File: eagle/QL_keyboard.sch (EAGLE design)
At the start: 42 parts, among them J1 USB-A-S, J2 AVR_SPI_PRG_6TESTPOINTS, U2 3.3V/150mA, U3 MAX3421ESMD, U4 ATMEGA328P_TQFP, U5 TXB0108PW-TSSOP20, Y1 8MHZ

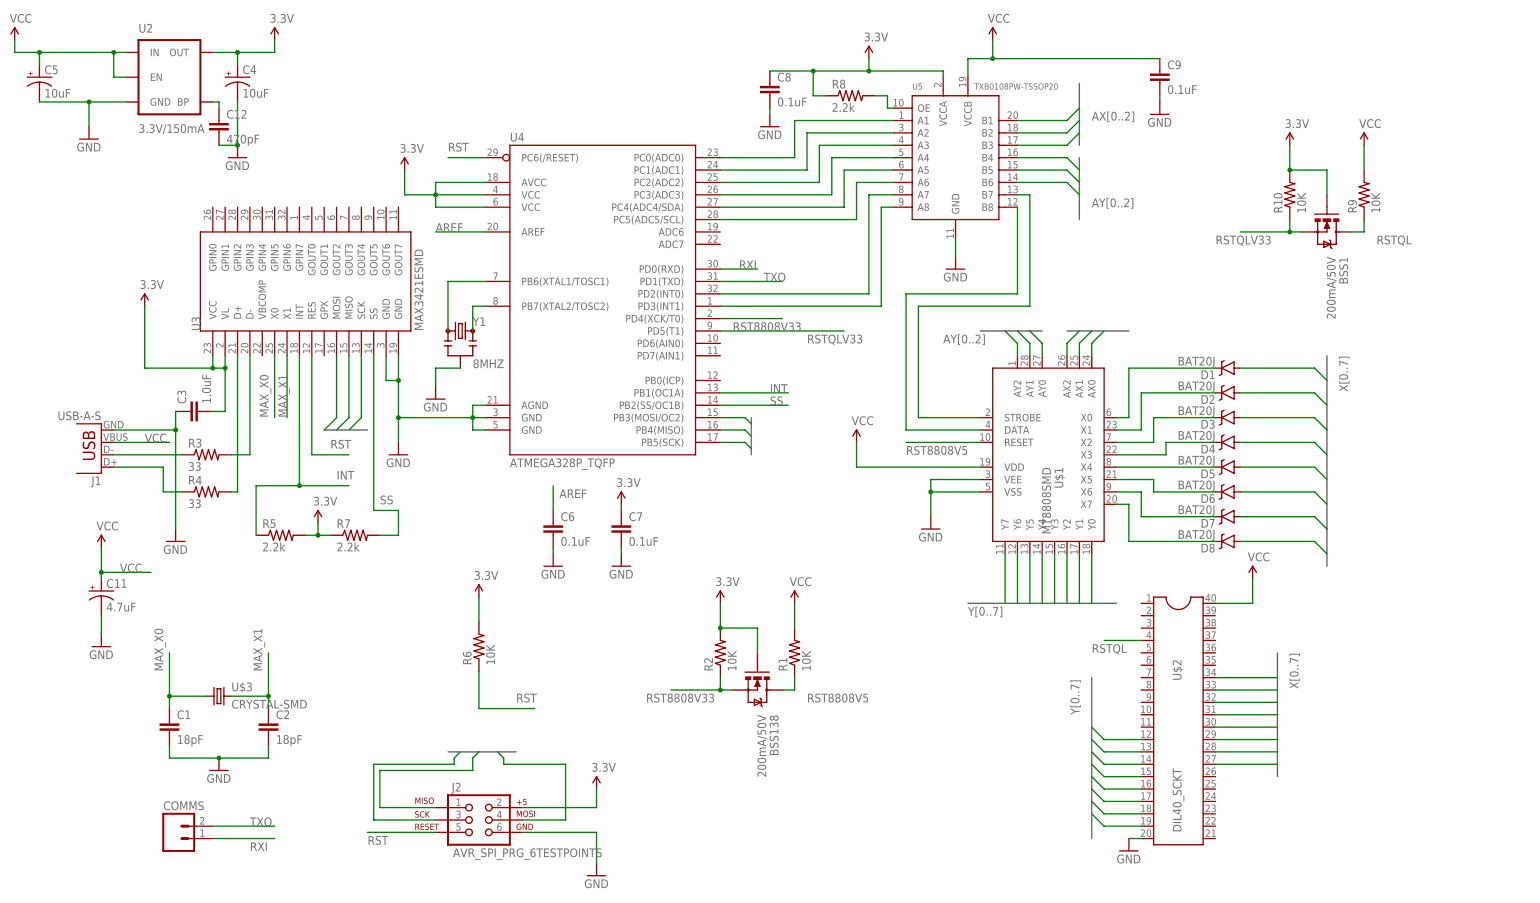
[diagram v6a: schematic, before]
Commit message: Minor routing adjustments
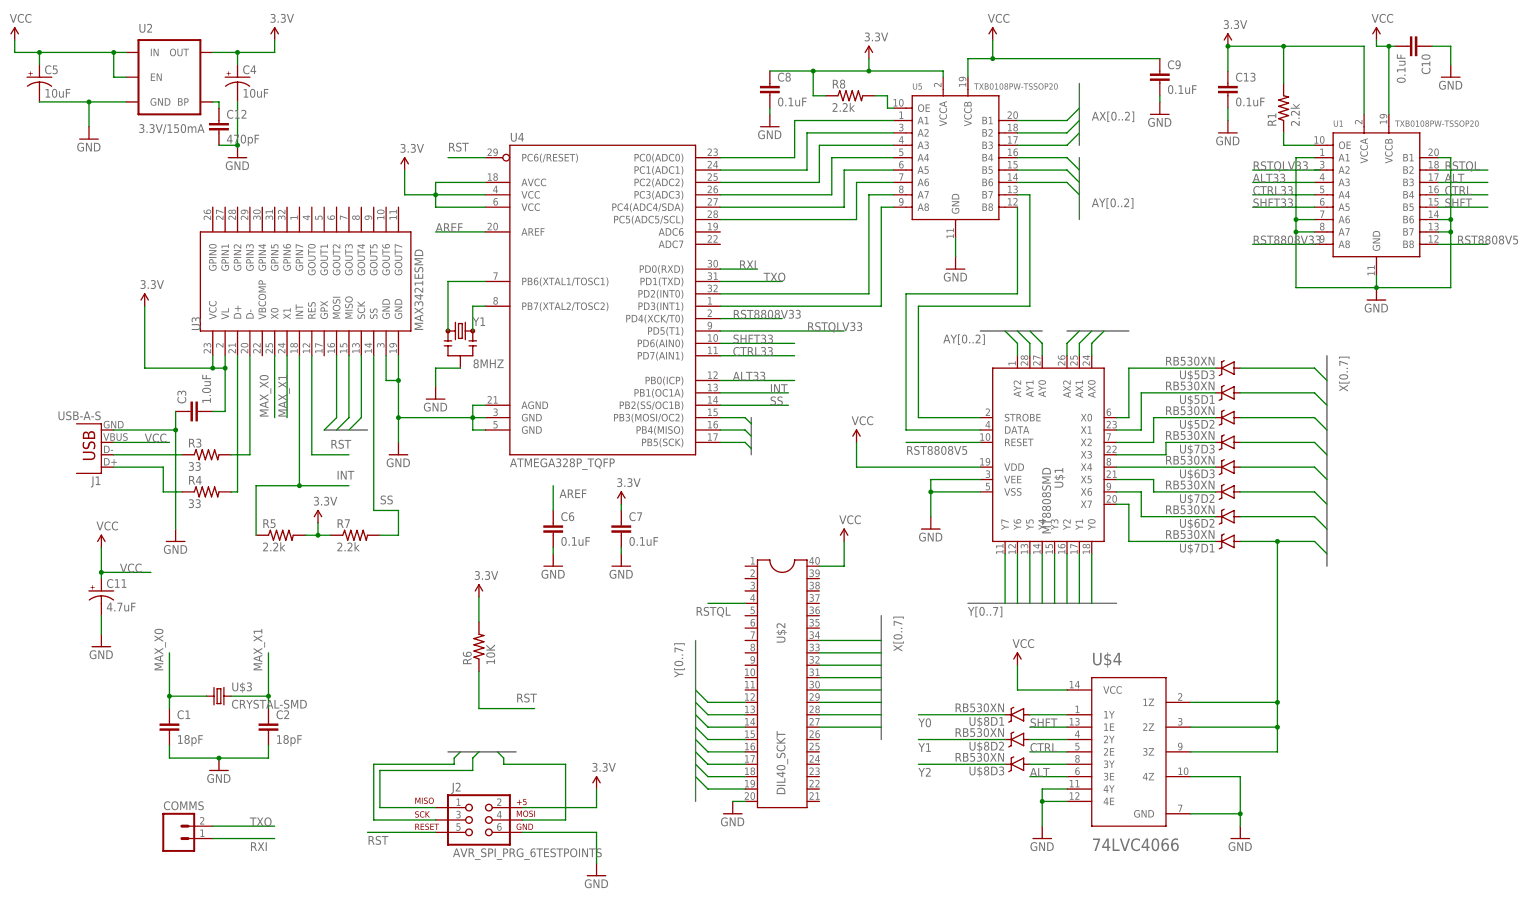
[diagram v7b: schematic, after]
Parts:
- removed BSS1, BSS138: 200mA/50V, SparkFun-DiscreteSemi:MOSFET-NCHANNELBSS138
- removed D1, D2, D3, D4, D5, D6, D7, D8: BAT20J, SparkFun-DiscreteSemi:DIODE-SCHOTTKY-BAT20J
- removed R10, R2, R9: 10K, SparkFun-Resistors:10KOHM-1/10W-1%(0603)0603
- added C10, C13: 0.1uF, SparkFun-Capacitors:2.2UF-10V-20%(0603)
- added U$4: 74LVC4066, ppe_custom:74LVC4066
- added U$5, U$6, U$7, U$8: RB530XN, ppe_custom:RB530XN
- added U1: TXB0108PW-TSSOP20, Seeed-OPL-ic:LOGIC-TXB0108PW(TSSOP20)
- R1: value 10K -> 2.2k; device SparkFun-Resistors:10KOHM-1/10W-1%(0603)0603 -> SparkFun-Resistors:2.2KOHM-1/10W-1%(0603)
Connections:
- new net ALT: U$4.3E, U1.B3
- new net ALT33: U1.A3, U4.PB0(ICP)
- new net CTRL: U$4.2E, U1.B4
- new net CTRL33: U1.A4, U4.PD7(AIN1)
- new net N$27: U$4.1Y, U$8D1.A
- new net N$28: U$4.2Y, U$8D2.A
- new net N$29: U$4.3Y, U$8D3.A
- new net N$31: R1.1, U1.OE
- new net SHFT: U$4.1E, U1.B5
- new net SHFT33: U1.A5, U4.PD6(AIN0)
- net 3.3V: now also C13.1, R1.2, U1.VCCA; no longer BSS1.G, BSS138.G, R10.2, R2.2
- net GND: now also C10.1, C13.2, U$4.4E, U$4.4Y, U$4.4Z, U$4.GND, U1.A1, U1.A6, U1.A7, U1.B1, U1.B6, U1.B7, U1.GND
- net N$19: now also U$5D3.C; no longer D1.C
- net N$20: now also U$5D1.C; no longer D2.C
- net N$21: now also U$5D2.C; no longer D3.C
- net N$22: now also U$7D3.C; no longer D4.C
- net N$23: now also U$6D3.C; no longer D5.C
- net N$24: now also U$7D2.C; no longer D6.C
- net N$25: now also U$6D2.C; no longer D7.C
- net N$26: now also U$7D1.C; no longer D8.C
- net RST8808V33: now also U1.A8; no longer BSS138.S, R2.1
- net RST8808V5: now also U1.B8; no longer BSS138.D, R1.1
- net RSTQL: now also U1.B2; no longer BSS1.D, R9.1
- net RSTQLV33: no longer BSS1.S, R10.1
- net VCC: now also C10.2, U$4.VCC, U1.VCCB; no longer R1.2, R9.2
- net X0: now also U$5D3.A; no longer D1.A
- net X1: now also U$5D1.A; no longer D2.A
- net X2: now also U$5D2.A; no longer D3.A
- net X3: now also U$7D3.A; no longer D4.A
- net X4: now also U$6D3.A; no longer D5.A
- net X5: now also U$7D2.A; no longer D6.A
- net X6: now also U$6D2.A; no longer D7.A
- net X7: now also U$4.1Z, U$4.2Z, U$4.3Z, U$7D1.A; no longer D8.A
- net Y0: now also U$8D1.C
- net Y1: now also U$8D2.C
- net Y2: now also U$8D3.C
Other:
- moved on the sheet: R1, U$2
